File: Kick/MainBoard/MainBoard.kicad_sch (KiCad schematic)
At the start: 33 parts, among them J1 CN1 / J11, J2 CN2 / J12, U0 NOIP1SN1300A-QTI, U1 NOIP1SN1300A-QTI, U2 NX3L4053, U3 NX3L4053, U4 MIC5504-1.8YM5

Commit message: routed 0 side on MainBoard with TFMLs
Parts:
- removed CD1, CD10, CD11, CD2, CD3, CD4, CD5, CD6, CD7, CD8, CD9: 100nF, Capacitor_SMD:C_0603_1608Metric, symbol Device:C
- removed R1: 47k, Resistor_SMD:R_0603_1608Metric, symbol Device:R
- removed U0: NOIP1SN1300A-QTI, NOIP1SN1300A-QTI:LCC101P1422X1422X228-48N, symbol NOIP1SN1300A-QTI:NOIP1SN1300A-QTI
- added J3: Conn_02x15_Odd_Even, SAMTEC_TFML11502LDLC:SAMTEC_TFML-115-02-L-D-LC, symbol Connector_Generic:Conn_02x15_Odd_Even
- added J4: Conn_02x10_Odd_Even, SAMTEC_TFML11002LDLC:SAMTEC_TFML-110-02-L-D-LC-TR, symbol Connector_Generic:Conn_02x10_Odd_Even
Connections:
- net GND: now also J3.10 (Pin_10), J3.12 (Pin_12), J3.14 (Pin_14), J3.16 (Pin_16), J3.18 (Pin_18), J3.2 (Pin_2), J3.20 (Pin_20), J3.22 (Pin_22), J3.24 (Pin_24), J3.26 (Pin_26), J3.28 (Pin_28), J3.30 (Pin_30), J3.4 (Pin_4), J3.6 (Pin_6), J3.8 (Pin_8), J4.10 (Pin_10), J4.19 (Pin_19), J4.20 (Pin_20)
- net clkout0_N: now also J3.3 (Pin_3)
- net clkout0_P: now also J3.5 (Pin_5)
- net dout0_0_N: now also J3.7 (Pin_7)
- net dout0_0_P: now also J3.9 (Pin_9)
- net dout1_0_N: now also J3.11 (Pin_11)
- net dout1_0_P: now also J3.13 (Pin_13)
- net dout2_0_N: now also J3.15 (Pin_15)
- net dout2_0_P: now also J3.17 (Pin_17)
- net dout3_0_N: now also J3.19 (Pin_19)
- net dout3_0_P: now also J3.21 (Pin_21)
- net miso: now also J4.4 (Pin_4)
- net monitor0_0: now also J4.3 (Pin_3)
- net monitor1_0: now also J4.1 (Pin_1)
- net mosi: now also J4.6 (Pin_6)
- net noip_clk_0: now also J1.17 (Pin_17), J4.13 (Pin_13); no longer J1.13 (Pin_13)
- net resetn_0: now also J4.5 (Pin_5)
- net sck: now also J4.2 (Pin_2)
- net ss_0: now also J4.8 (Pin_8)
- net sync0_N: now also J3.23 (Pin_23)
- net sync0_P: now also J3.25 (Pin_25)
- net trigger0_0: now also J1.13 (Pin_13), J4.7 (Pin_7); no longer J1.17 (Pin_17)
- net vdd18_0: now also J4.15 (Pin_15)
- net vdd33_0: now also J4.11 (Pin_11)
- net vddpix_0: now also J4.9 (Pin_9)
- no-connect marks 92 -> 96

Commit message: routed bottom part with length matching
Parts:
- removed CD12, CD13, CD14, CD15, CD16, CD17, CD18, CD19, CD20, CD21, CD22: 100nF, Capacitor_SMD:C_0603_1608Metric, symbol Device:C
- removed R2: 47k, Resistor_SMD:R_0603_1608Metric, symbol Device:R
- removed U1: NOIP1SN1300A-QTI, NOIP1SN1300A-QTI:LCC101P1422X1422X228-48N, symbol NOIP1SN1300A-QTI:NOIP1SN1300A-QTI
- added J5: Conn_02x15_Odd_Even, SAMTEC_TFML11502LDLC:SAMTEC_TFML-115-02-L-D-LC, symbol Connector_Generic:Conn_02x15_Odd_Even
- added J6: Conn_02x10_Odd_Even, SAMTEC_TFML11002LDLC:SAMTEC_TFML-110-02-L-D-LC-TR, symbol Connector_Generic:Conn_02x10_Odd_Even
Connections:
- net GND: now also J5.10 (Pin_10), J5.12 (Pin_12), J5.14 (Pin_14), J5.16 (Pin_16), J5.18 (Pin_18), J5.2 (Pin_2), J5.20 (Pin_20), J5.22 (Pin_22), J5.24 (Pin_24), J5.26 (Pin_26), J5.28 (Pin_28), J5.30 (Pin_30), J5.4 (Pin_4), J5.6 (Pin_6), J5.8 (Pin_8), J6.19 (Pin_19), J6.20 (Pin_20); no longer J4.10 (Pin_10)
- net clkout1_N: now also J5.3 (Pin_3)
- net clkout1_P: now also J5.5 (Pin_5)
- net dout0_1_N: now also J5.7 (Pin_7)
- net dout0_1_P: now also J5.9 (Pin_9)
- net dout1_1_N: now also J5.11 (Pin_11)
- net dout1_1_P: now also J5.13 (Pin_13)
- net dout2_1_N: now also J5.15 (Pin_15)
- net dout2_1_P: now also J5.17 (Pin_17)
- net dout3_1_N: now also J5.19 (Pin_19)
- net dout3_1_P: now also J5.21 (Pin_21)
- net miso: now also J6.4 (Pin_4)
- net monitor0_1: now also J1.41 (Pin_41), J6.3 (Pin_3); no longer J1.33 (Pin_33)
- net monitor1_1: now also J1.39 (Pin_39), J6.1 (Pin_1); no longer J1.31 (Pin_31)
- net mosi: now also J6.6 (Pin_6)
- net noip_clk_1: now also J1.47 (Pin_47), J6.13 (Pin_13); no longer J1.37 (Pin_37)
- net resetn_1: now also J1.43 (Pin_43), J6.5 (Pin_5); no longer J1.29 (Pin_29)
- net sck: now also J6.2 (Pin_2)
- net ss_1: now also J6.8 (Pin_8)
- net sw_~{E}_1: now also J1.37 (Pin_37); no longer J1.47 (Pin_47)
- net sync1_N: now also J5.23 (Pin_23)
- net sync1_P: now also J5.25 (Pin_25)
- net trigger0_1: now also J1.45 (Pin_45), J6.7 (Pin_7); no longer J1.39 (Pin_39)
- net vdd18_1: now also J6.15 (Pin_15)
- net vdd18_toggle_1: now also J1.29 (Pin_29); no longer J1.41 (Pin_41)
- net vdd33_1: now also J6.11 (Pin_11)
- net vdd33_toggle_1: now also J1.31 (Pin_31); no longer J1.43 (Pin_43)
- net vddpix_1: now also J6.9 (Pin_9)
- net vddpix_toggle_1: now also J1.33 (Pin_33); no longer J1.45 (Pin_45)
- no-connect marks 96 -> 102

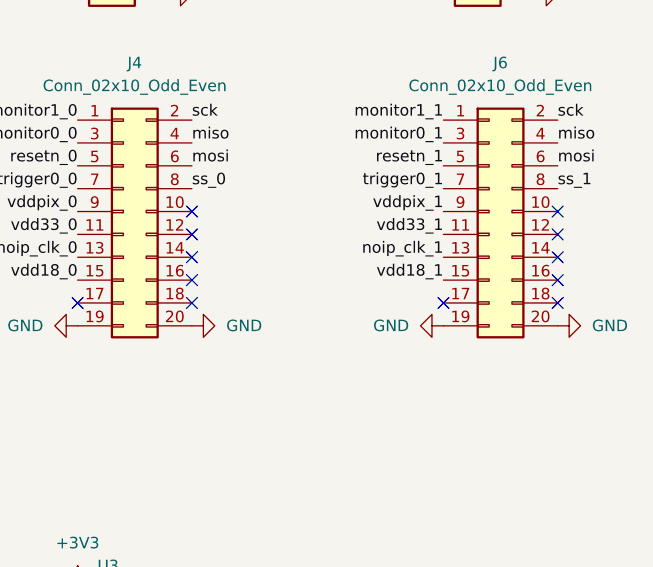
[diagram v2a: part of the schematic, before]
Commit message: routed all layers, length matched top part and updated models
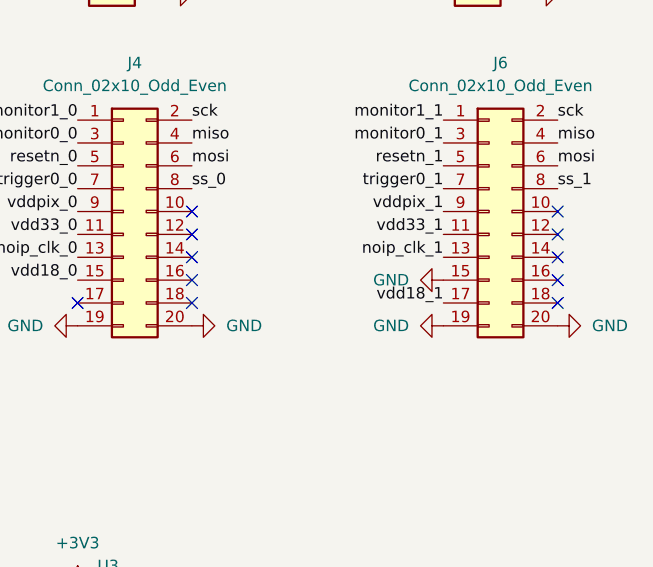
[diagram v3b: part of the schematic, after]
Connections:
- net GND: now also J6.15 (Pin_15)
- net vdd18_1: now also J6.17 (Pin_17); no longer J6.15 (Pin_15)
- no-connect marks 102 -> 101
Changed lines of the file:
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@@
 	)
 	(no_connect
-		(at 171.45 113.03)
-	)
-	(no_connect
 		(at 184.15 102.87)
 	)
@@
 		)
 	)
+	(label "vdd18_1"
+		(at 171.45 113.03 180)
+		(fields_autoplaced yes)
+		(effects
+			(font
+				(size 1.27 1.27)
+			)
+			(justify right bottom)
+		)
+	)
 	(label "vddpix_toggle_0"
 		(at 80.01 177.8 180)
@@
 		)
 	)
-	(label "vdd18_1"
-		(at 171.45 110.49 180)
-		(fields_autoplaced yes)
-		(effects
-			(font
-				(size 1.27 1.27)
-			)
-			(justify right bottom)
-		)
-	)
 	(label "sw_~{E}_0"
 		(at 100.33 162.56 0)
@@
 					(unit 1)
 				)
+			)
+		)
+	)
+	(symbol
+		(lib_id "power:GND")
+		(at 171.45 110.49 270)
+		(unit 1)
+		(exclude_from_sim no)
+		(in_bom yes)
+		(on_board yes)
+		(dnp no)
+		(fields_autoplaced yes)
+		(property "Reference" "#PWR077"
+			(at 165.1 110.49 0)
+			(effects
+				(font
+					(size 1.27 1.27)
+				)
+				(hide yes)
+			)
+		)
+		(property "Value" "GND"
+			(at 167.64 110.4899 90)
+			(effects
+				(font
+					(size 1.27 1.27)
+				)
+				(justify right)
+			)
+		)
+		(property "Footprint" ""
+			(at 171.45 110.49 0)
+			(effects
+				(font
+					(size 1.27 1.27)
+				)
+				(hide yes)
+			)
+		)
+		(property "Datasheet" ""
+			(at 171.45 110.49 0)
+			(effects
+				(font
+					(size 1.27 1.27)
+				)
+				(hide yes)
+			)
+		)
+		(property "Description" "Power symbol creates a global label with name \"GND\" , ground"
+			(at 171.45 110.49 0)
+			(effects
+				(font
+					(size 1.27 1.27)
+				)
+				(hide yes)
+			)
+		)
+		(pin "1"
+		)
+		(instances
+			(project ""
+				(path "/277e05da-ccda-4679-9933-a39aa09eccc2"
+					(reference "#PWR077")
+					(unit 1)
+				)

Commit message: actual working commit
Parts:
- J1: LCSC Part (none) -> TFM-140-12-L-D-A
- J2: LCSC Part (none) -> TFML-140-12-L-D-A
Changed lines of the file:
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@@
 			)
 		)
+		(property "LCSC Part" "TFM-140-12-L-D-A"
+			(at 49.53 86.36 0)
+			(effects
+				(font
+					(size 1.27 1.27)
+				)
+				(hide yes)
+			)
+		)
 		(pin "59"
 		)
@@
 			(at 92.71 85.09 0)
 			(effects
+				(font
+					(size 1.27 1.27)
+				)
+				(hide yes)
+			)
+		)
+		(property "LCSC Part" "TFML-140-12-L-D-A"
+			(at 92.71 85.09 0)
+			(effects

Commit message: new design and PCB with available clock pins and LED pins. Still cross-domain timing issues.
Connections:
- net clkout0_N: now also J2.48 (Pin_48); no longer J2.22 (Pin_22)
- net clkout0_P: now also J2.46 (Pin_46); no longer J2.24 (Pin_24)
- net dout0_0_N: now also J2.22 (Pin_22); no longer J2.26 (Pin_26)
- net dout0_0_P: now also J2.24 (Pin_24); no longer J2.28 (Pin_28)
- net dout1_0_N: now also J2.26 (Pin_26); no longer J2.32 (Pin_32)
- net dout1_0_P: now also J2.28 (Pin_28); no longer J2.34 (Pin_34)
- net dout2_0_N: now also J2.32 (Pin_32); no longer J2.36 (Pin_36)
- net dout2_0_P: now also J2.34 (Pin_34); no longer J2.38 (Pin_38)
- net dout3_0_N: now also J2.36 (Pin_36); no longer J2.42 (Pin_42)
- net dout3_0_P: now also J2.38 (Pin_38); no longer J2.44 (Pin_44)
- net miso: now also J1.30 (Pin_30); no longer J1.36 (Pin_36)
- net monitor1_1: now also J1.37 (Pin_37); no longer J1.39 (Pin_39)
- net mosi: now also J1.32 (Pin_32); no longer J1.38 (Pin_38)
- net sck: now also J1.28 (Pin_28), J1.38 (Pin_38); no longer J1.32 (Pin_32), J1.42 (Pin_42)
- net ss_0: now also J1.22 (Pin_22); no longer J1.28 (Pin_28)
- net ss_1: now also J1.36 (Pin_36); no longer J1.40 (Pin_40)
- net sw_~{E}_1: now also J1.26 (Pin_26); no longer J1.37 (Pin_37)
- net sync0_N: now also J2.42 (Pin_42); no longer J2.46 (Pin_46)
- net sync0_P: now also J2.44 (Pin_44); no longer J2.48 (Pin_48)
